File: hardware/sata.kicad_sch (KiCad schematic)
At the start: 18 parts, among them IC1 ASM1061, J5 SATA, J8 SATA Power, Y1 Crystal

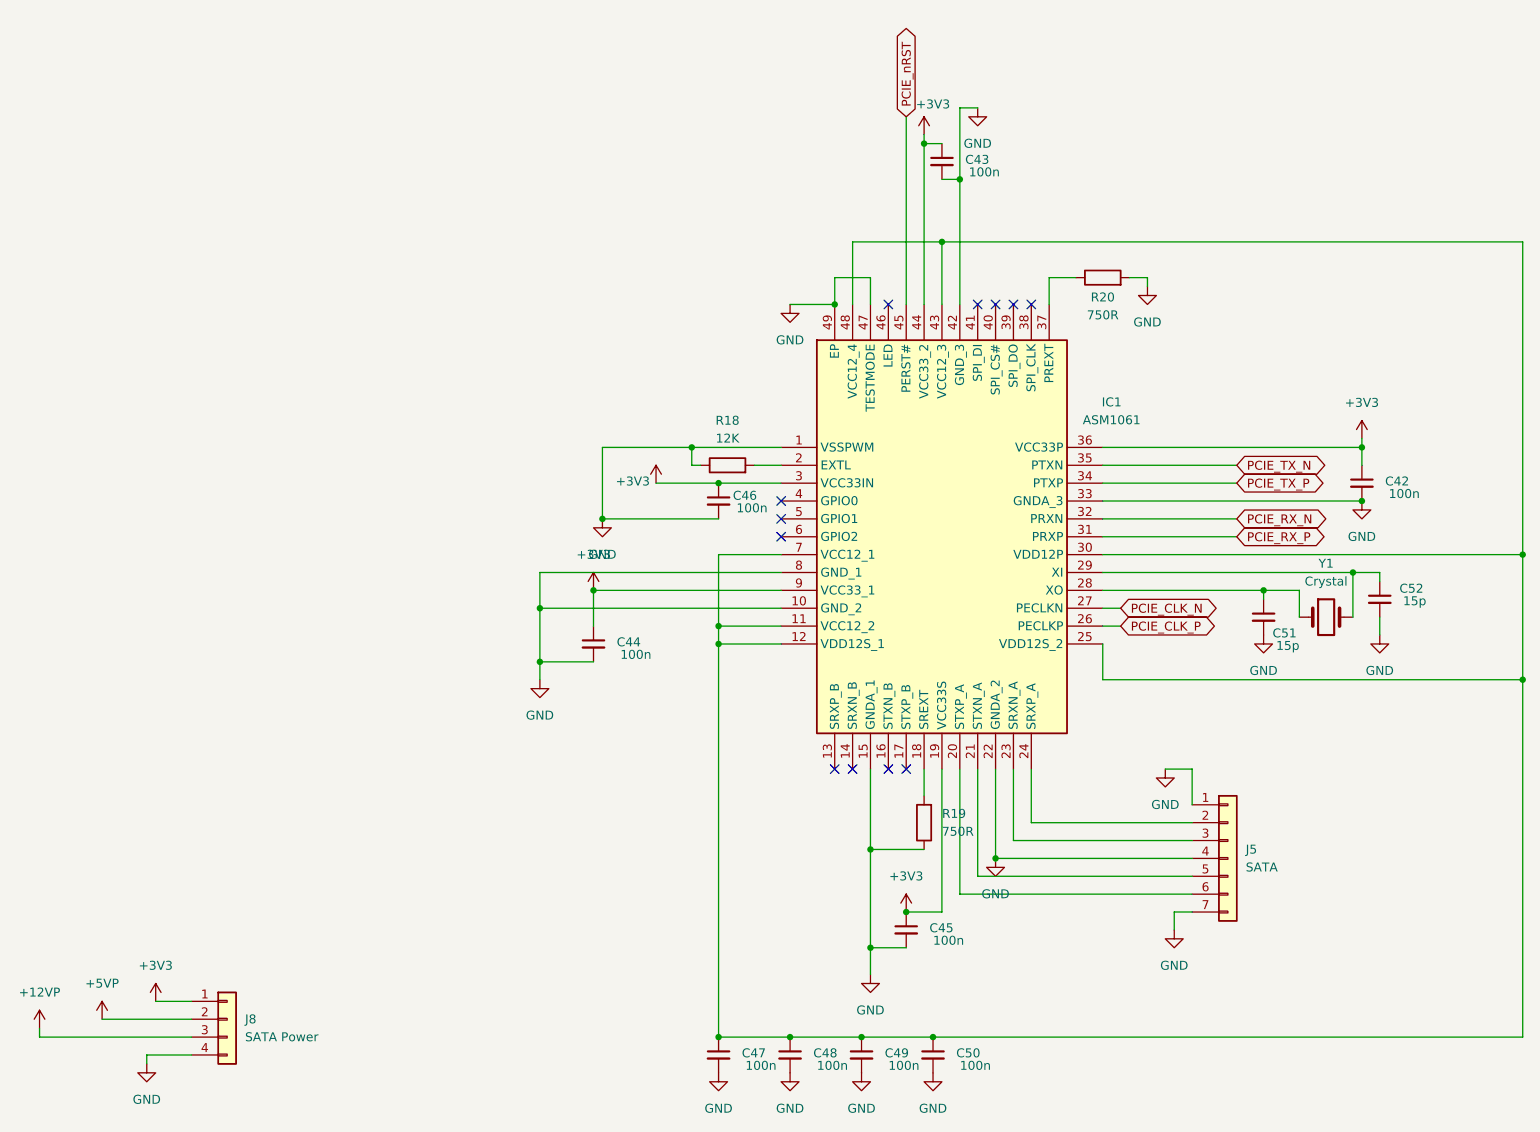
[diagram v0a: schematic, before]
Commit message: Reannotate all components sequentially
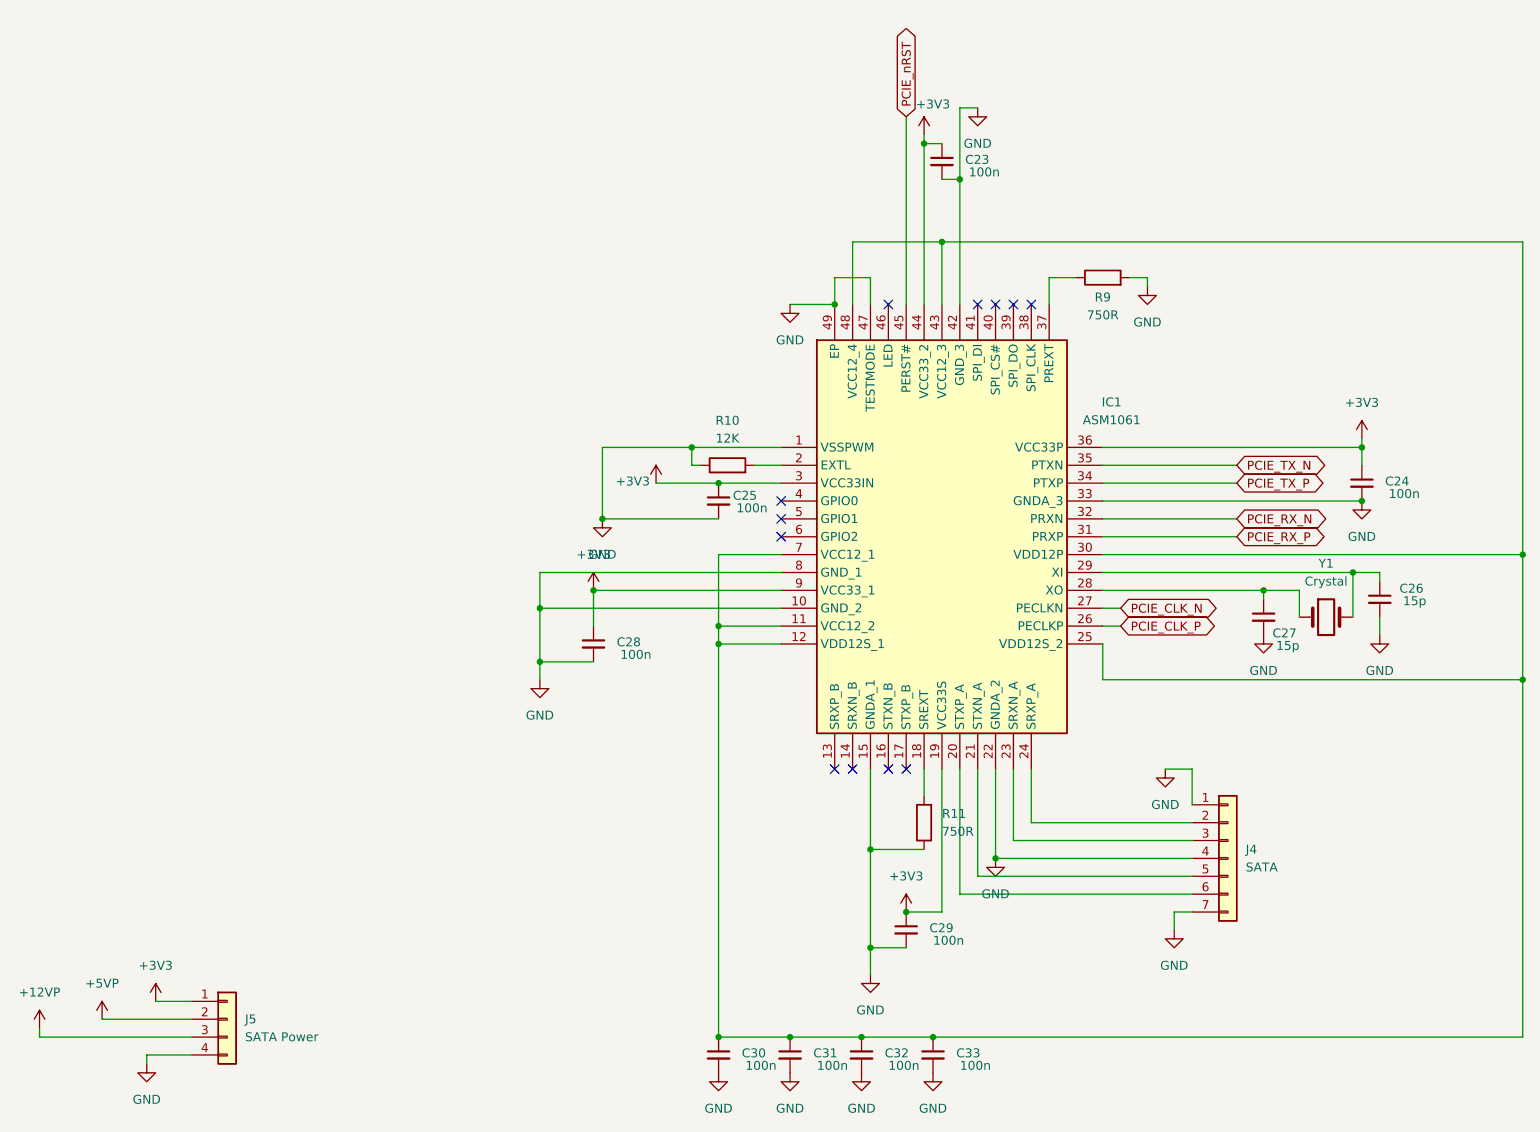
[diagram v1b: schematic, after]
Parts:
- renumbered C43 to C23, C42 to C24, C46 to C25, C52 to C26, C51 to C27, C44 to C28, C45 to C29, C47 to C30, C48 to C31, C49 to C32, C50 to C33, J5 to J4, J8 to J5, R18 to R10, R19 to R11, R20 to R9

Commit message: Assign footprints to all components
All components now have valid footprints:
- 0805 for all resistors, caps, LEDs
- SOT-23-5/6 for ICs
- 2512 SMD fuse, 3215 crystal
- Pin headers, USB-C, solder jumper, battery holder
- ERC: 0 errors, 0 warnings
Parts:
- J4: footprint (none) -> Connector_PinHeader_2.54mm:PinHeader_1x07_P2.54mm_Vertical
- J5: footprint (none) -> Connector_PinHeader_2.54mm:PinHeader_1x04_P2.54mm_Vertical
- R10, R11, R9: footprint (none) -> Resistor_SMD:R_0805_2012Metric
- Y1: footprint (none) -> Crystal:Crystal_SMD_3215-2Pin_3.2x1.5mm
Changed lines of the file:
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@@
 			)
 		)
-		(property "Footprint" ""
+		(property "Footprint" "Connector_PinHeader_2.54mm:PinHeader_1x04_P2.54mm_Vertical"
 			(at 43.18 157.48 0)
 			(hide yes)
@@
 			)
 		)
-		(property "Footprint" ""
+		(property "Footprint" "Crystal:Crystal_SMD_3215-2Pin_3.2x1.5mm"
 			(at 199.39 100.33 0)
 			(hide yes)
@@
 			)
 		)
-		(property "Footprint" ""
+		(property "Footprint" "Resistor_SMD:R_0805_2012Metric"
 			(at 114.3 80.518 90)
 			(hide yes)
@@
 			)
 		)
-		(property "Footprint" ""
+		(property "Footprint" "Resistor_SMD:R_0805_2012Metric"
 			(at 144.018 129.54 90)
 			(hide yes)
@@
 			)
 		)
-		(property "Footprint" ""
+		(property "Footprint" "Resistor_SMD:R_0805_2012Metric"
 			(at 167.64 53.848 90)
 			(hide yes)
@@
 			)
 		)
-		(property "Footprint" ""
+		(property "Footprint" "Connector_PinHeader_2.54mm:PinHeader_1x07_P2.54mm_Vertical"
 			(at 185.42 134.62 0)
 			(hide yes)

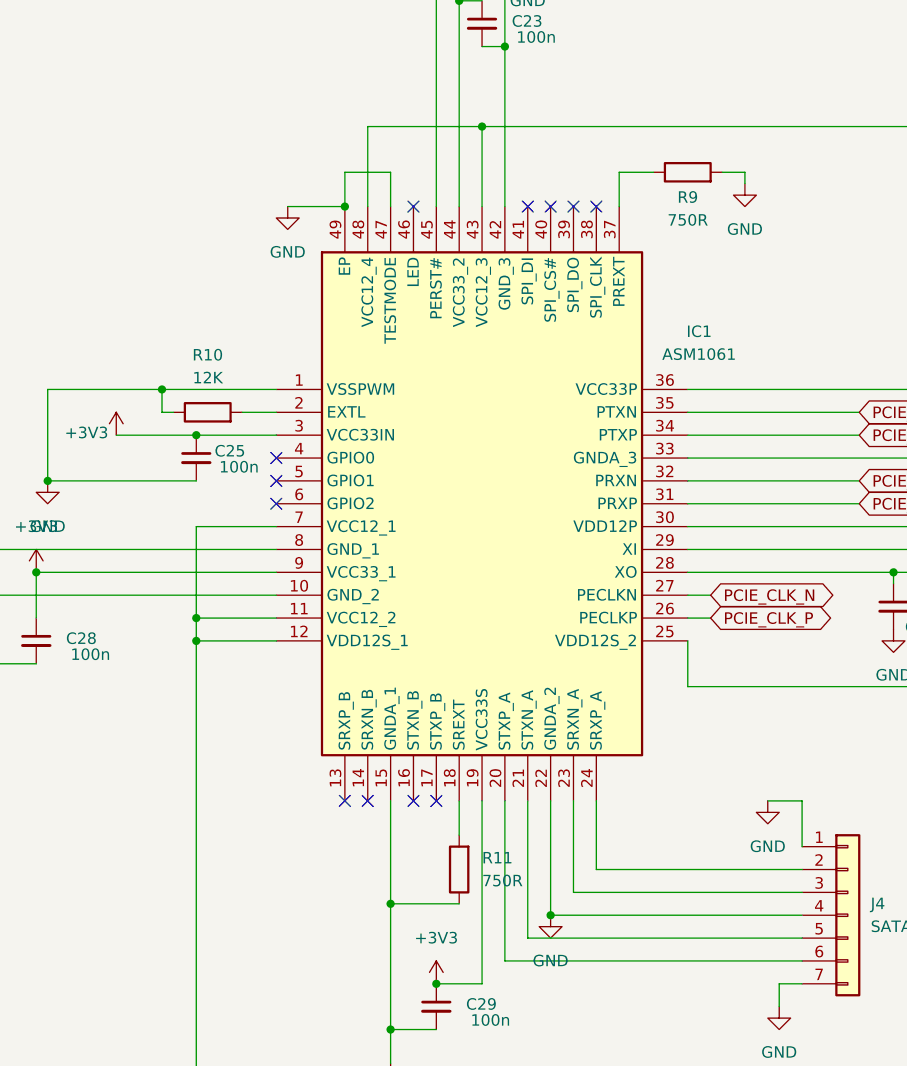
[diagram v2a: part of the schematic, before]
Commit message: Standardize all resistors to R_Small, fix broken R22 connection
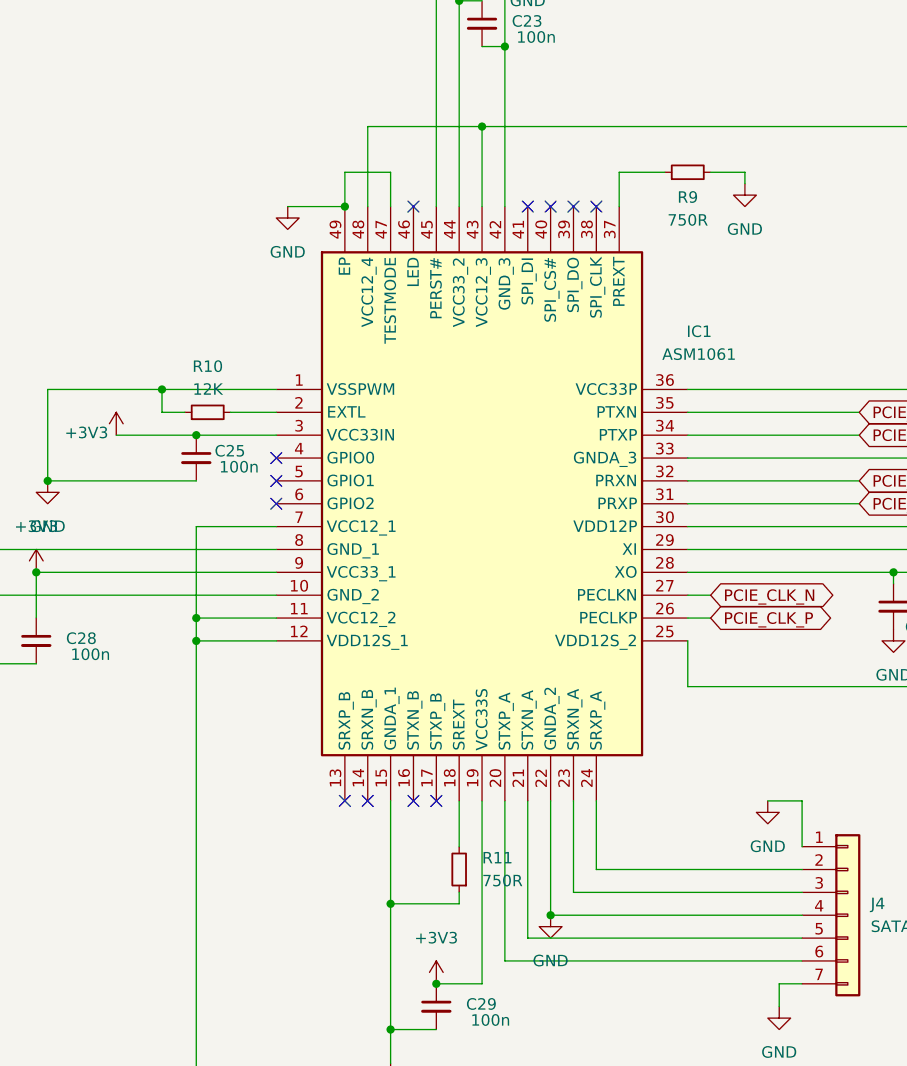
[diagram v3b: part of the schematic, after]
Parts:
- R10, R11, R9: symbol Device:R -> Device:R_Small
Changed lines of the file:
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@@
 	(wire
 		(pts
-			(xy 171.45 52.07) (xy 173.99 52.07)
-		)
-		(stroke
-			(width 0)
-			(type default)
-		)
-	)
-	(wire
-		(pts
 			(xy 134.62 52.07) (xy 129.54 52.07)
 		)
@@
 	(wire
 		(pts
-			(xy 142.24 121.92) (xy 142.24 125.73)
+			(xy 142.24 121.92) (xy 142.24 127)
 		)
 		(stroke
@@
 	(wire
 		(pts
+			(xy 170.18 52.07) (xy 173.99 52.07)
+		)
+		(stroke
+			(width 0)
+			(type default)
+		)
+	)
+	(wire
+		(pts
 			(xy 134.62 147.32) (xy 139.7 147.32)
 		)
@@
 	(wire
 		(pts
-			(xy 160.02 52.07) (xy 163.83 52.07)
+			(xy 160.02 52.07) (xy 165.1 52.07)
 		)
 		(stroke
@@
 	(wire
 		(pts
-			(xy 110.49 78.74) (xy 109.22 78.74)
+			(xy 109.22 78.74) (xy 111.76 78.74)
 		)
 		(stroke
@@
 	(wire
 		(pts
+			(xy 116.84 78.74) (xy 121.92 78.74)
+		)
+		(stroke
+			(width 0)
+			(type default)
+		)
+	)
+	(wire
+		(pts
 			(xy 157.48 121.92) (xy 157.48 129.54)
 		)
@@
 	(wire
 		(pts
-			(xy 143.51 160.02) (xy 227.33 160.02)
+			(xy 142.24 132.08) (xy 142.24 133.35)
 		)
 		(stroke
@@
 	(wire
 		(pts
-			(xy 113.03 91.44) (xy 113.03 101.6)
+			(xy 143.51 160.02) (xy 227.33 160.02)
 		)
 		(stroke
@@
 	(wire
 		(pts
-			(xy 31.75 162.56) (xy 31.75 163.83)
+			(xy 113.03 91.44) (xy 113.03 101.6)
 		)
 		(stroke
@@
 	(wire
 		(pts
-			(xy 118.11 78.74) (xy 121.92 78.74)
+			(xy 31.75 162.56) (xy 31.75 163.83)
 		)
 		(stroke
@@
 	)
 	(symbol
-		(lib_id "Device:R")
+		(lib_id "Device:R_Small")
 		(at 114.3 78.74 90)
 		(unit 1)
@@
 		(fields_autoplaced yes)
 		(property "Reference" "R10"
-			(at 114.3 72.39 90)
+			(at 114.3 73.66 90)
 			(show_name no)
 			(do_not_autoplace no)
@@
 		)
 		(property "Value" "12K"
-			(at 114.3 74.93 90)
+			(at 114.3 76.2 90)
 			(show_name no)
 			(do_not_autoplace no)
@@
 		)
 		(property "Footprint" "Resistor_SMD:R_0805_2012Metric"
-			(at 114.3 80.518 90)
+			(at 114.3 78.74 0)
 			(hide yes)
 			(show_name no)
@@
 			)
 		)
-		(property "Description" "Resistor"
+		(property "Description" "Resistor, small symbol"
 			(at 114.3 78.74 0)
 			(hide yes)
@@
 	)
 	(symbol
-		(lib_id "Device:R")
+		(lib_id "Device:R_Small")
 		(at 142.24 129.54 180)
 		(unit 1)
@@
 		)
 		(property "Footprint" "Resistor_SMD:R_0805_2012Metric"
-			(at 144.018 129.54 90)
+			(at 142.24 129.54 0)
 			(hide yes)
 			(show_name no)
@@
 			)
 		)
-		(property "Description" "Resistor"
+		(property "Description" "Resistor, small symbol"
 			(at 142.24 129.54 0)
 			(hide yes)
@@
 	)
 	(symbol
-		(lib_id "Device:R")
+		(lib_id "Device:R_Small")
 		(at 167.64 52.07 90)
 		(unit 1)
@@
 		)
 		(property "Footprint" "Resistor_SMD:R_0805_2012Metric"
-			(at 167.64 53.848 90)
+			(at 167.64 52.07 0)
 			(hide yes)
 			(show_name no)
@@
 			)
 		)
-		(property "Description" "Resistor"
+		(property "Description" "Resistor, small symbol"
 			(at 167.64 52.07 0)
 			(hide yes)
